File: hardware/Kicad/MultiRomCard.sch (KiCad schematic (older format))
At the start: 9 parts, among them P1 VC4000_Cartridge_Bus, U1 Arduino_UNO, U2 74HC595, U3 74HC595, U4 74HC595, U5 6264, U6 74HC245, U7 74HC245, U8 74HC245

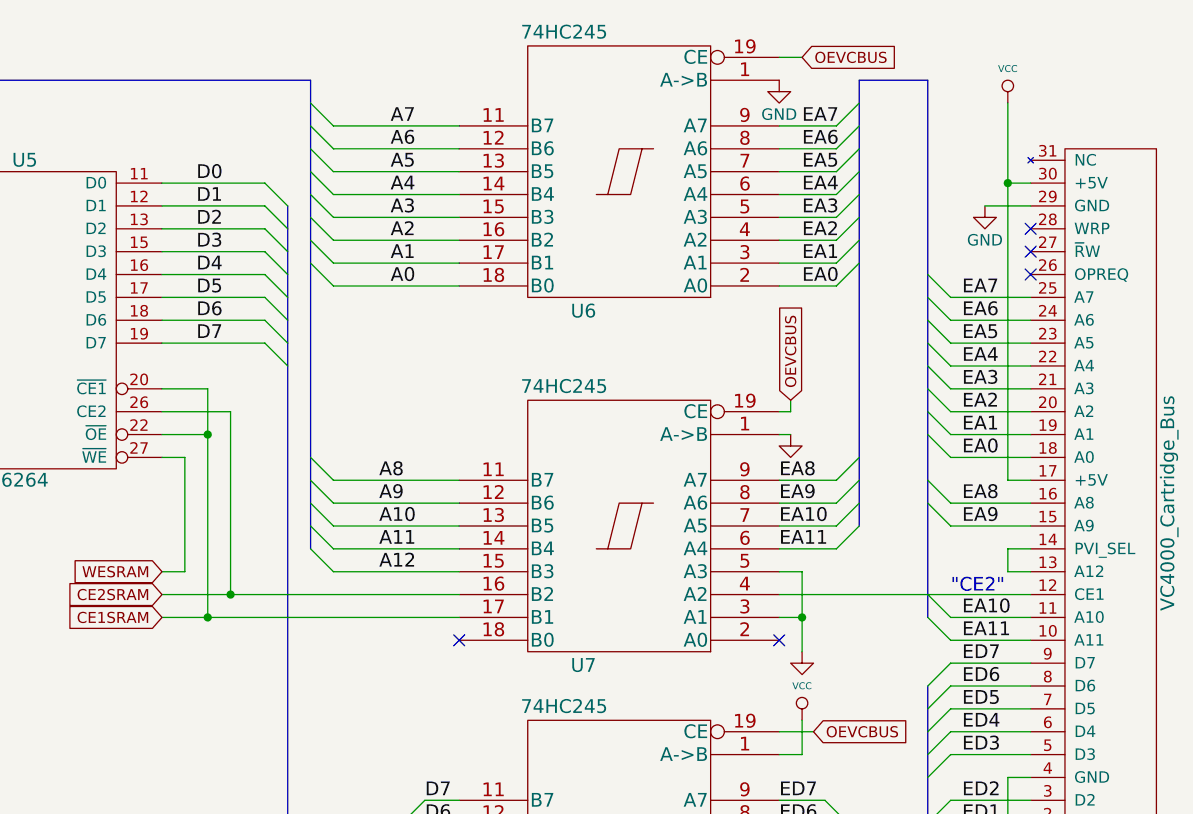
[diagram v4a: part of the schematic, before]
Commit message: Move "CE2" track to another BT pin and remove special.lib.
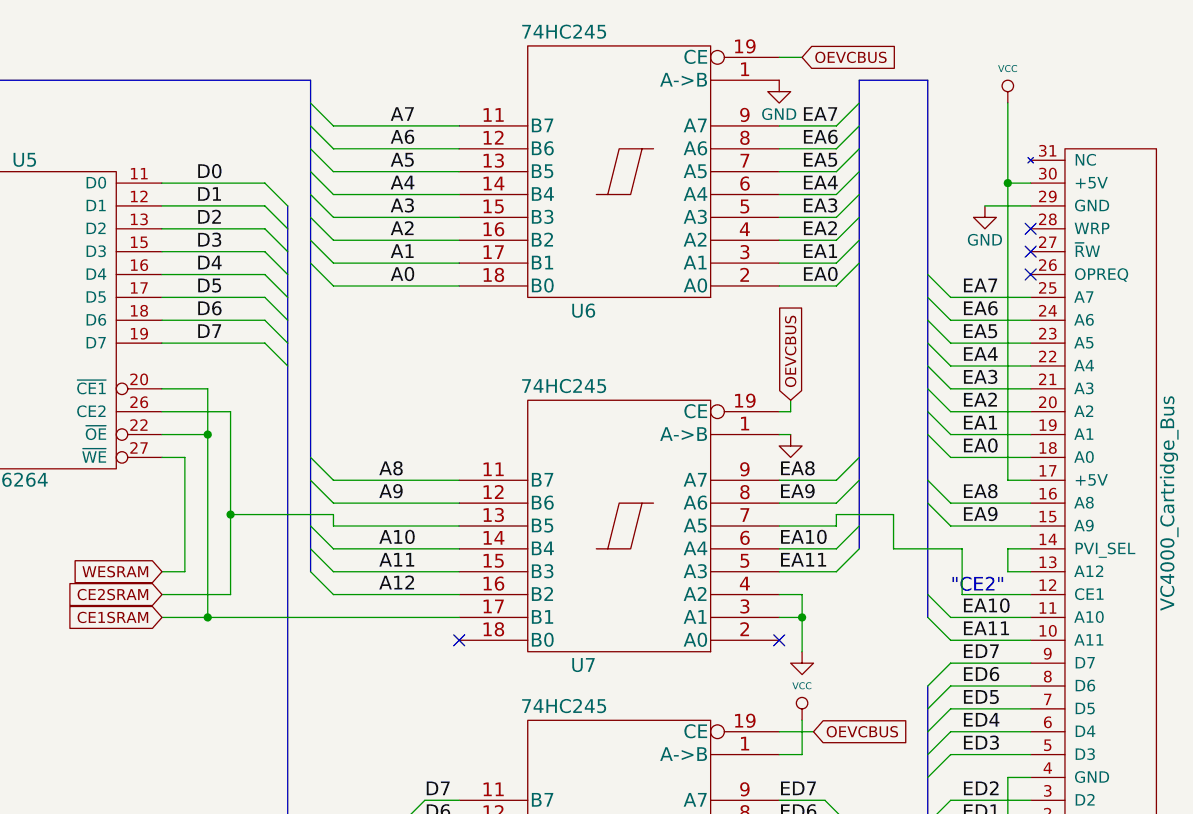
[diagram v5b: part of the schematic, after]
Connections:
- net A10: now also U7.14 (B4); no longer U7.13 (B5)
- net A11: now also U7.15 (B3); no longer U7.14 (B4)
- net A12: now also U7.16 (B2); no longer U7.15 (B3)
- net CE2SRAM: now also U7.13 (B5); no longer U7.16 (B2)
- net EA10: now also U7.6 (A4); no longer U7.7 (A5)
- net EA11: now also U7.5 (A3); no longer U7.6 (A4)
- net GND: now also U7.4 (A2); no longer U7.5 (A3)
- net at P1.12 (CE1): now also U7.7 (A5); no longer U7.4 (A2)
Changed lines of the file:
@@
 LIBS:memory
 LIBS:xilinx
-LIBS:special
 LIBS:microcontrollers
 LIBS:dsp
@@
 	7400 3250 7500 3350
 Entry Wire Line
-	7400 3350 7500 3450
-Entry Wire Line
 	7400 3450 7500 3550
 Entry Wire Line
 	7400 3550 7500 3650
+Entry Wire Line
+	7400 3650 7500 3750
 Text Label 7750 2400 0    60   ~ 0
 A0
@@
 Text Label 7700 3350 0    60   ~ 0
 A9
-Text Label 7700 3450 0    60   ~ 0
+Text Label 7700 3550 0    60   ~ 0
 A10
-Text Label 7700 3550 0    60   ~ 0
+Text Label 7700 3650 0    60   ~ 0
 A11
-Text Label 7700 3650 0    60   ~ 0
+Text Label 7700 3750 0    60   ~ 0
 A12
 NoConn ~ 8050 3950
@@
 	9700 3350 9800 3250
 Entry Wire Line
-	9700 3450 9800 3350
-Entry Wire Line
 	9700 3550 9800 3450
+Entry Wire Line
+	9700 3650 9800 3550
 Entry Wire Line
 	10100 2450 10200 2550
@@
 Text Label 9450 3350 0    60   ~ 0
 EA9
-Text Label 9450 3450 0    60   ~ 0
+Text Label 9450 3550 0    60   ~ 0
 EA10
-Text Label 9450 3550 0    60   ~ 0
+Text Label 9450 3650 0    60   ~ 0
 EA11
 Entry Wire Line
@@
 	7500 3350 8050 3350
 Wire Wire Line
-	7500 3450 8050 3450
-Wire Wire Line
-	7500 3550 8050 3550
-Wire Wire Line
 	7500 2400 8050 2400
 Wire Wire Line
@@
 Wire Wire Line
 	7500 1700 8050 1700
-Wire Wire Line
-	7500 3650 8050 3650
-Wire Bus Line
-	7400 1500 7400 3550
+Wire Bus Line
+	7400 1500 7400 3650
 Wire Wire Line
 	6750 3150 6850 3150
@@
 Wire Wire Line
 	9450 3350 9700 3350
-Wire Wire Line
-	9450 3450 9700 3450
-Wire Wire Line
-	9450 3550 9700 3550
 Wire Bus Line
 	5150 1500 7400 1500
@@
 	10100 1500 9800 1500
 Wire Bus Line
-	9800 1500 9800 3450
+	9800 1500 9800 3550
 Wire Wire Line
 	9450 4650 9650 4650
@@
 	6850 3650 6750 3650
 Wire Wire Line
-	6750 3750 8050 3750
-Wire Wire Line
 	6750 3850 8050 3850
 Wire Wire Line
-	9550 3650 9550 4000
+	9550 3750 9550 4000
 Wire Wire Line
 	9550 3850 9450 3850
 Wire Wire Line
-	9450 3750 10550 3750
-Wire Wire Line
 	10550 3550 10450 3550
 Wire Wire Line
@@
 Wire Wire Line
 	10450 3650 10550 3650
-Wire Wire Line
-	9450 3650 9550 3650
 Connection ~ 9550 3850
 Wire Bus Line
@@
 Wire Wire Line
 	7050 2950 7050 3750
-Connection ~ 7050 3750
 Wire Wire Line
 	10350 2050 10550 2050
@@
 Wire Wire Line
 	9450 3050 9500 3050
+Wire Wire Line
+	7050 3750 6750 3750
+Wire Wire Line
+	8050 3750 7500 3750
+Wire Wire Line
+	8050 3650 7500 3650
+Wire Wire Line
+	7500 3550 8050 3550
+Wire Wire Line
+	9550 3750 9450 3750
+Wire Wire Line
+	9450 3650 9700 3650
+Wire Wire Line
+	9450 3550 9700 3550
+Wire Wire Line
+	10550 3750 10250 3750
+Wire Wire Line
+	10250 3750 10250 3550
+Wire Wire Line
+	10250 3550 9950 3550
+Wire Wire Line
+	9950 3550 9950 3400
+Wire Wire Line
+	9950 3400 9700 3400
+Wire Wire Line
+	9700 3400 9700 3450
+Wire Wire Line
+	9700 3450 9450 3450
+Wire Wire Line
+	8050 3450 7500 3450
+Wire Wire Line
+	7500 3450 7500 3400
+Wire Wire Line
+	7500 3400 7050 3400
+Connection ~ 7050 3400
 $EndSCHEMATC

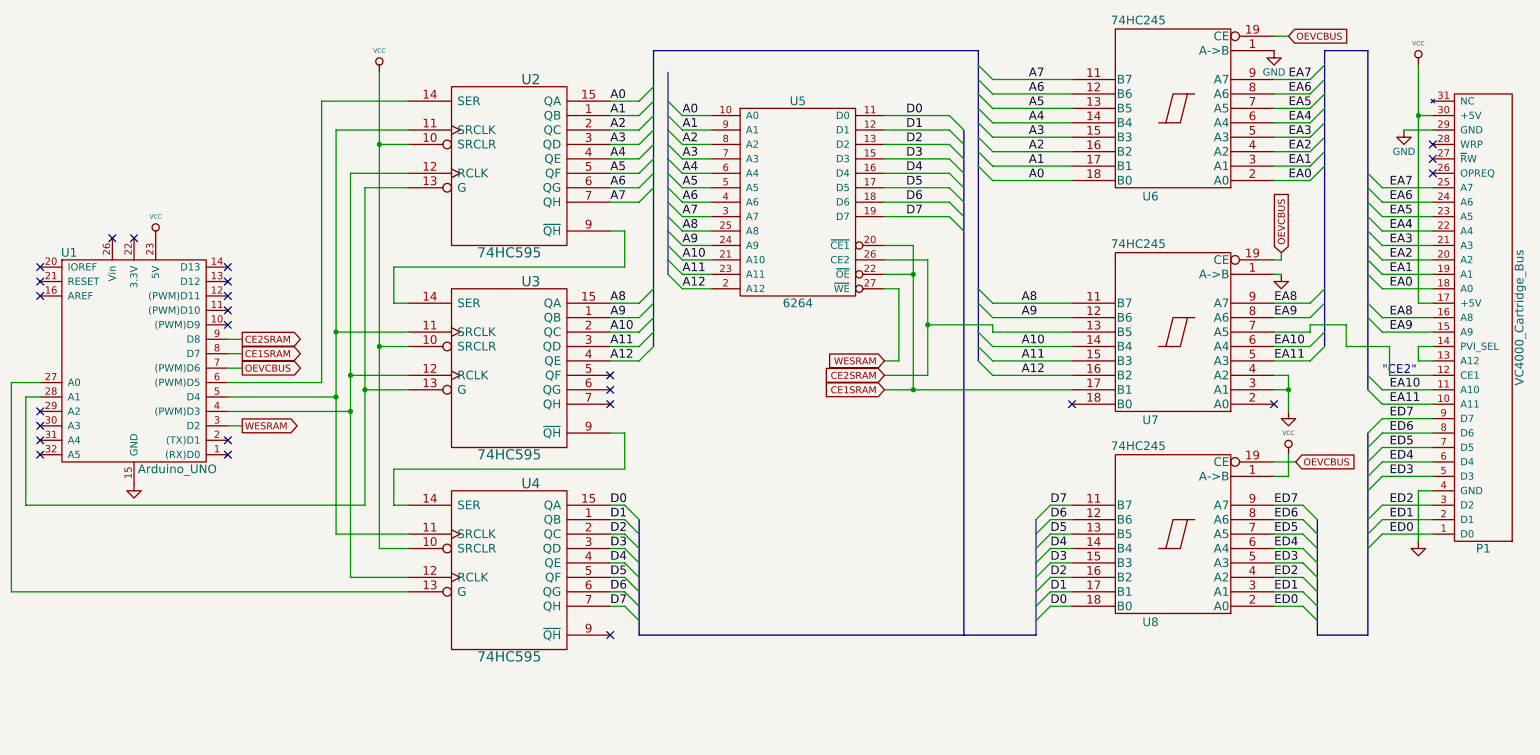
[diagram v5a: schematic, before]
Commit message: Updated SVG schematic.
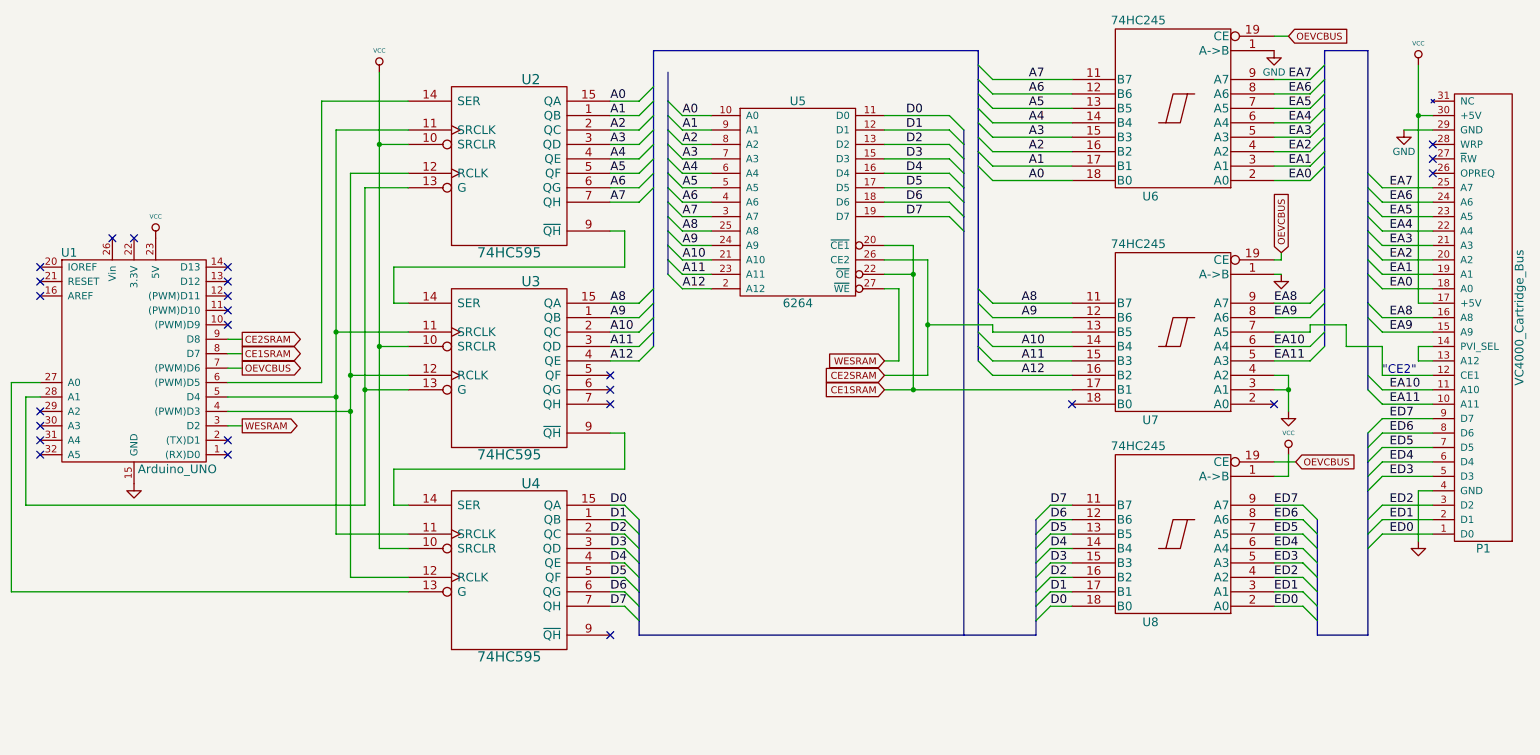
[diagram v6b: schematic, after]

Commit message: [SCH] Corrected an error with the internal address bus.
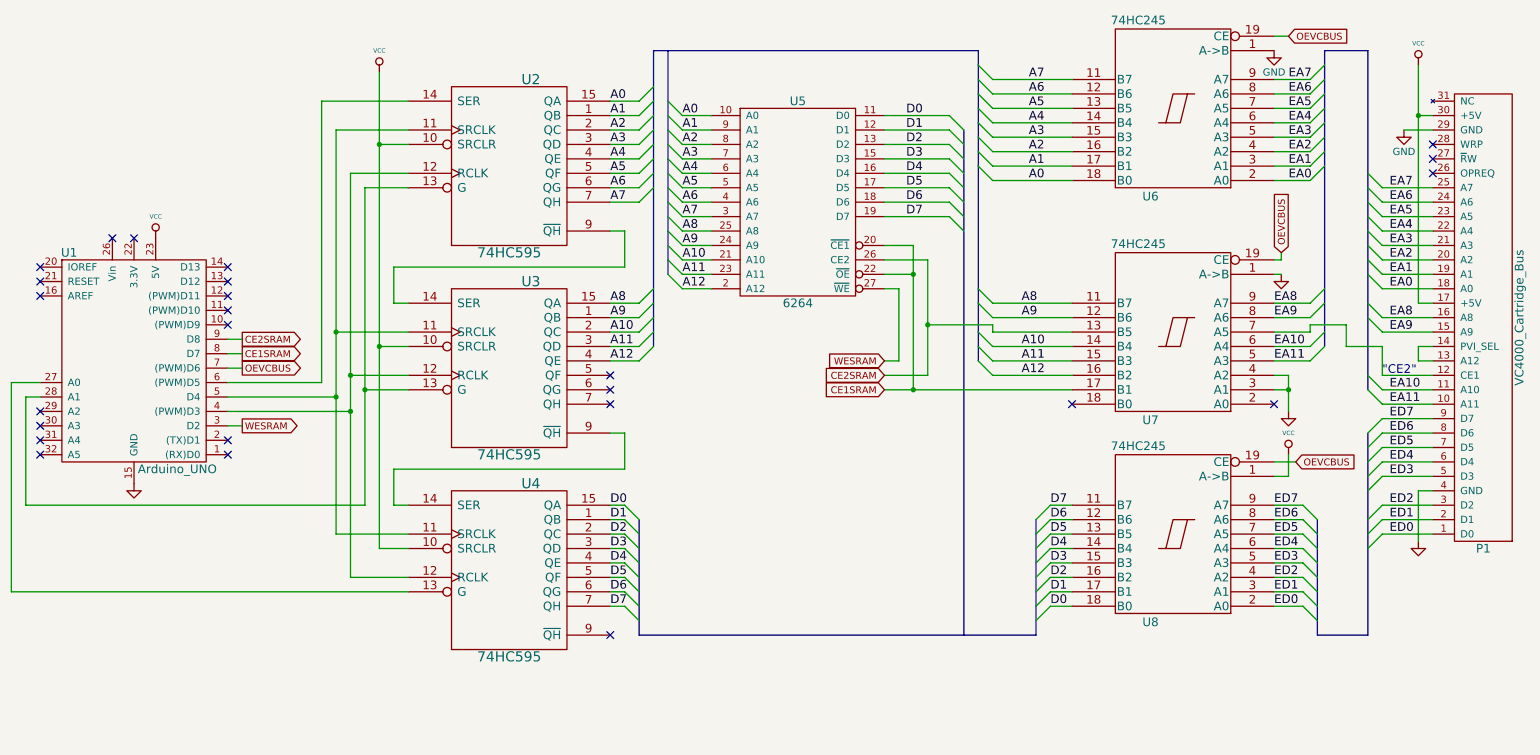
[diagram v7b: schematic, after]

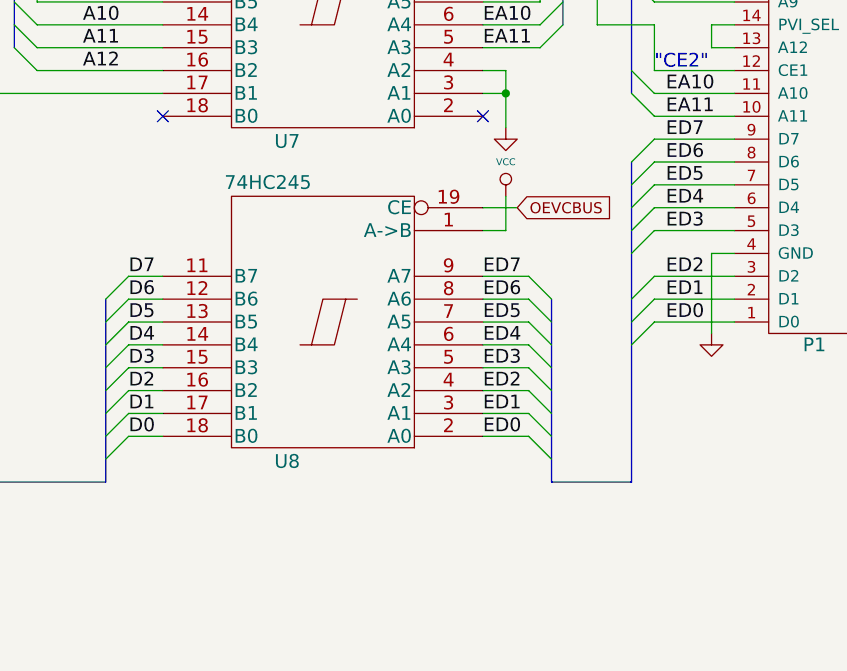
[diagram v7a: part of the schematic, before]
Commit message: [SCH/PCB] Added IC power decoupling caps.
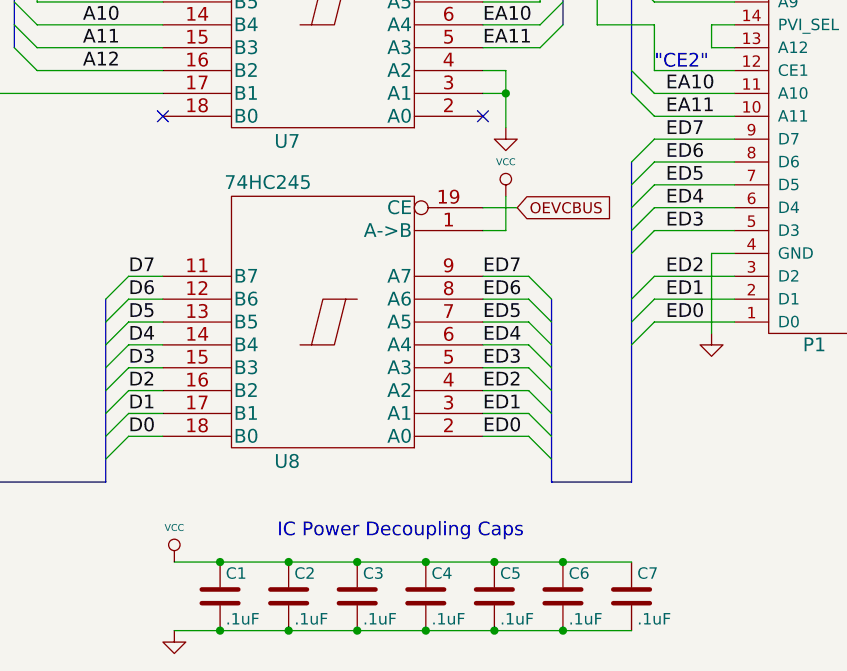
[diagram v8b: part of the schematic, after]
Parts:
- added C1, C2, C3, C4, C5, C6, C7: .1uF, Capacitors_ThroughHole:C_Disc_D6_P5, symbol C
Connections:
- net GND: now also C1.2, C2.2, C3.2, C4.2, C5.2, C6.2, C7.2
- net VCC: now also C1.1, C2.1, C3.1, C4.1, C5.1, C6.1, C7.1
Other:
- note added: "IC Power Decoupling Caps"
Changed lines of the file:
@@
 	10450 3250 10550 3250
 Wire Bus Line
-	10100 5550 9750 5550
+	9750 5550 10100 5550
 Wire Wire Line
 	2200 3800 2850 3800
@@
 	10100 4750 10200 4650
 Wire Bus Line
-	10100 4150 10100 5550
+	10100 5550 10100 4150
 Wire Wire Line
 	9500 2950 9450 2950
@@
 	7500 3400 7050 3400
 Connection ~ 7050 3400
+$Comp
+L C C1
+U 1 1 55855363
+P 8300 6050
+F 0 "C1" H 8325 6150 50  0000 L CNN
+F 1 ".1uF" H 8325 5950 50  0000 L CNN
+F 2 "Capacitors_ThroughHole:C_Disc_D6_P5" H 8338 5900 30  0001 C CNN
+F 3 "" H 8300 6050 60  0000 C CNN
+	1    8300 6050
+	1    0    0    -1
+$EndComp
+$Comp
+L C C2
+U 1 1 558556DE
+P 8600 6050
+F 0 "C2" H 8625 6150 50  0000 L CNN
+F 1 ".1uF" H 8625 5950 50  0000 L CNN
+F 2 "Capacitors_ThroughHole:C_Disc_D6_P5" H 8638 5900 30  0001 C CNN
+F 3 "" H 8600 6050 60  0000 C CNN
+	1    8600 6050
+	1    0    0    -1
+$EndComp
+$Comp
+L C C3
+U 1 1 55855710
+P 8900 6050
+F 0 "C3" H 8925 6150 50  0000 L CNN
+F 1 ".1uF" H 8925 5950 50  0000 L CNN
+F 2 "Capacitors_ThroughHole:C_Disc_D6_P5" H 8938 5900 30  0001 C CNN
+F 3 "" H 8900 6050 60  0000 C CNN
+	1    8900 6050
+	1    0    0    -1
+$EndComp
+$Comp
+L C C4
+U 1 1 55855748
+P 9200 6050
+F 0 "C4" H 9225 6150 50  0000 L CNN
+F 1 ".1uF" H 9225 5950 50  0000 L CNN
+F 2 "Capacitors_ThroughHole:C_Disc_D6_P5" H 9238 5900 30  0001 C CNN
+F 3 "" H 9200 6050 60  0000 C CNN
+	1    9200 6050
+	1    0    0    -1
+$EndComp
+$Comp
+L C C5
+U 1 1 55855787
+P 9500 6050
+F 0 "C5" H 9525 6150 50  0000 L CNN
+F 1 ".1uF" H 9525 5950 50  0000 L CNN
+F 2 "Capacitors_ThroughHole:C_Disc_D6_P5" H 9538 5900 30  0001 C CNN
+F 3 "" H 9500 6050 60  0000 C CNN
+	1    9500 6050
+	1    0    0    -1
+$EndComp
+$Comp
+L C C6
+U 1 1 558557C4
+P 9800 6050
+F 0 "C6" H 9825 6150 50  0000 L CNN
+F 1 ".1uF" H 9825 5950 50  0000 L CNN
+F 2 "Capacitors_ThroughHole:C_Disc_D6_P5" H 9838 5900 30  0001 C CNN
+F 3 "" H 9800 6050 60  0000 C CNN
+	1    9800 6050
+	1    0    0    -1
+$EndComp
+$Comp
+L C C7
+U 1 1 55855806
+P 10100 6050
+F 0 "C7" H 10125 6150 50  0000 L CNN
+F 1 ".1uF" H 10125 5950 50  0000 L CNN
+F 2 "Capacitors_ThroughHole:C_Disc_D6_P5" H 10138 5900 30  0001 C CNN
+F 3 "" H 10100 6050 60  0000 C CNN
+	1    10100 6050
+	1    0    0    -1
+$EndComp
+Wire Wire Line
+	8100 5900 10100 5900
+Connection ~ 8600 5900
+Connection ~ 8900 5900
+Connection ~ 9200 5900
+Connection ~ 9500 5900
+Connection ~ 9800 5900
+Wire Wire Line
+	8100 6200 10100 6200
+Connection ~ 8600 6200
+Connection ~ 8900 6200
+Connection ~ 9200 6200
+Connection ~ 9500 6200
+Connection ~ 9800 6200
+$Comp
+L GND #PWR011
+U 1 1 558564D3
+P 8100 6200
+F 0 "#PWR011" H 8100 6200 30  0001 C CNN
+F 1 "GND" H 8100 6130 30  0001 C CNN
+F 2 "" H 8100 6200 60  0000 C CNN
+F 3 "" H 8100 6200 60  0000 C CNN
+	1    8100 6200
+	1    0    0    -1
+$EndComp
+$Comp
+L VCC #PWR012
+U 1 1 5585650E
+P 8100 5900
+F 0 "#PWR012" H 8100 6000 30  0001 C CNN
+F 1 "VCC" H 8100 6050 30  0000 C CNN
+F 2 "" H 8100 5900 60  0000 C CNN
+F 3 "" H 8100 5900 60  0000 C CNN
+	1    8100 5900
+	1    0    0    -1
+$EndComp
+Connection ~ 8300 5900
+Connection ~ 8300 6200
+Text Notes 8550 5800 0    60   ~ 0
+IC Power Decoupling Caps
 $EndSCHEMATC
